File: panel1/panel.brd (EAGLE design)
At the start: 50.1 x 50.4 mm, 31 parts, among them J1 AVR_SPI_PRG_62X3_LOCK, J3 AVR_SPI_PRG_62X3_LOCK

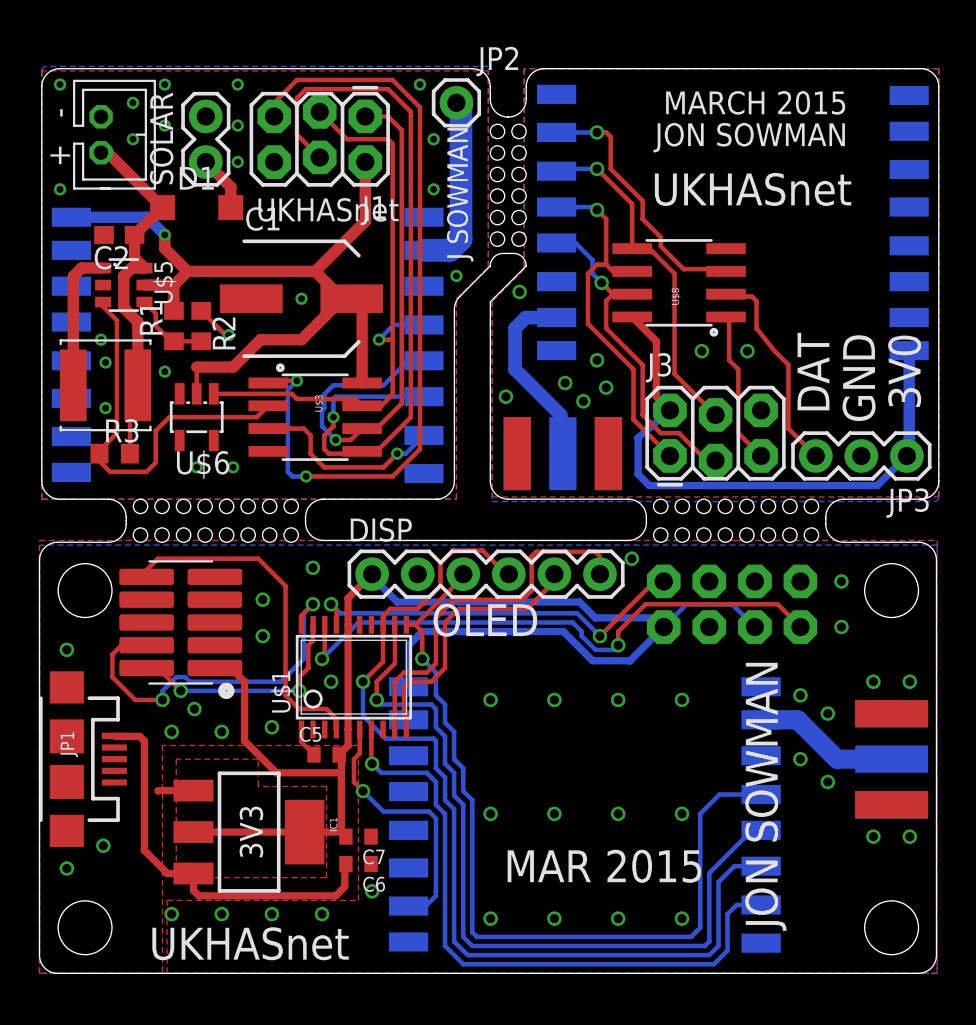
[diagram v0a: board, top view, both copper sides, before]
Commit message: added jumpers because dont trust ebay sellers
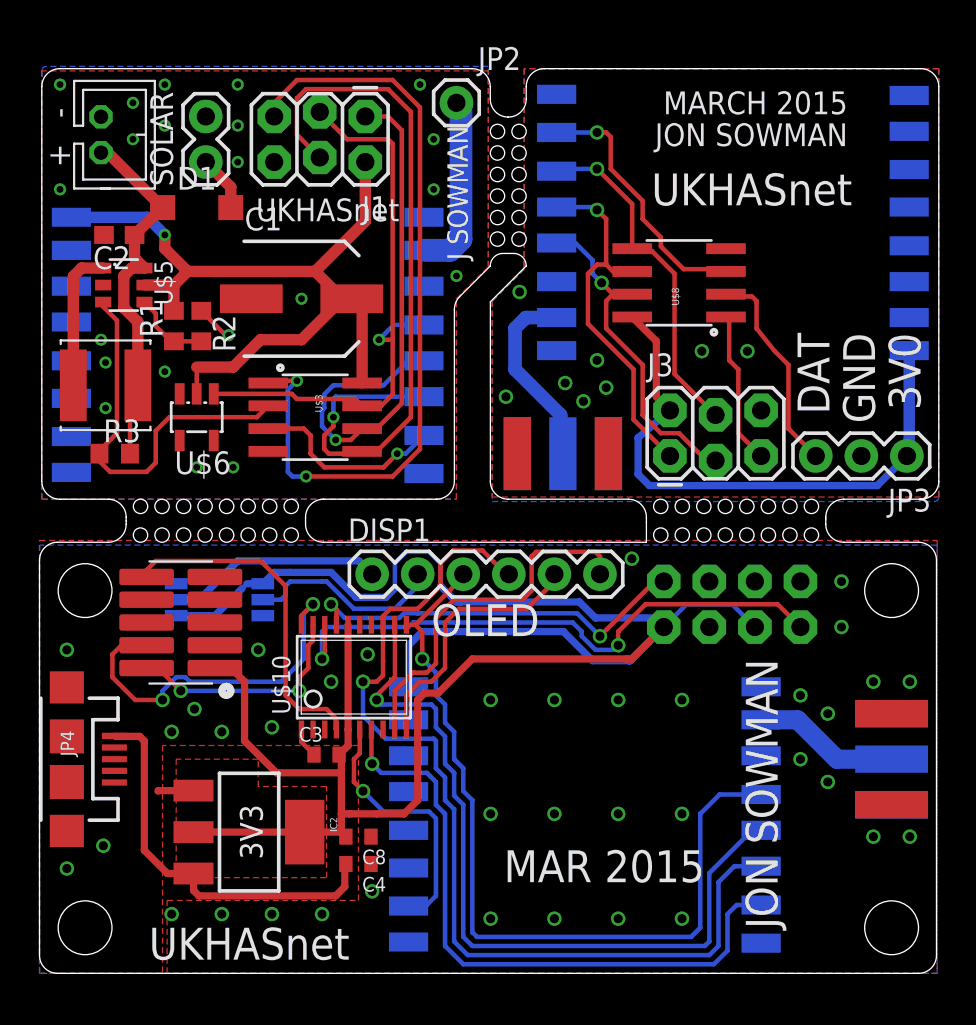
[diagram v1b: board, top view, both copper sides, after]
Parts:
- added SJ1, SJ2: (no value), SparkFun-Retired:SJ_3
- renumbered C5 to C3, C6 to C4, C7 to C8, DISP to DISP1, ESP8266 to ESP1, IC1 to IC2, J$1 to J$3, JP1 to JP4, U$1 to U$10, U$2 to U$11, U$4 to U$12
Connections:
- net DISPLAY_CS renamed DISPLAY_CS1
- net DISPLAY_DC renamed DISPLAY_DC1
- net DISPLAY_RST renamed DISPLAY_RST1
- net MISO renamed MISO3
- net MOSI renamed MOSI3
- net NRST renamed NRST1
- net RFM_CS renamed RFM_CS1
- net SCK renamed SCK2
- net SWCLK renamed SWCLK1
- net SWDAT renamed SWDAT1
- net UART_RX renamed UART_RX1
- net UART_TX renamed UART_TX1
- removed net GND: C3.1, C4.1, C8.1, DISP1.2, ESP1.2, IC2.1, J$3.GND@0, J$3.GND@1, J$3.GND@2, J$3.GND@3, JP4.GND, JP4.MT1, JP4.MT2, U$10.1, U$10.15, U$11.GNDA, U$11.GNDB, U$12.3, U$12.5, U$12.7, U$12.9
- removed net VCC: C3.2, C8.2, DISP1.1, ESP1.3, ESP1.7, IC2.2, IC2.4, U$10.16, U$10.5, U$11.VCC, U$12.1
- new net GND3: C3.1, C4.1, C8.1, ESP1.2, IC2.1, J$3.GND@0, J$3.GND@1, J$3.GND@2, J$3.GND@3, JP4.GND, JP4.MT1, JP4.MT2, SJ1.3, SJ2.3, U$10.1, U$10.15, U$11.GNDA, U$11.GNDB, U$12.3, U$12.5, U$12.7, U$12.9
- new net N$13: DISP1.2, SJ1.2
- new net N$14: DISP1.1, SJ2.2
- new net VCC3: C3.2, C8.2, ESP1.3, ESP1.7, IC2.2, IC2.4, SJ1.1, SJ2.1, U$10.16, U$10.5, U$11.VCC, U$12.1
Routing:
- net VCC3: track 0.00 -> 115.0 mm
- net VCC: track 77.2 -> 0.00 mm
- net N$14: track 0.00 -> 12.1 mm
- net N$13: track 0.00 -> 11.2 mm
- net GND3: track 0.00 -> 3.68 mm, vias 0 -> 38
- net GND: track 3.68 -> 0.00 mm, vias 39 -> 0
- net UART_RX1: track 32.3 -> 33.2 mm
- added copper zone on layer 1, net GND3
- added copper zone on layer 16, net GND3
- added copper zone on layer 1, net VCC3
- removed copper zone on layer 1, net GND
- removed copper zone on layer 16, net GND
- removed copper zone on layer 1, net VCC
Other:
- outline, holes or cut-outs redrawn
- board text added: "P1"
- board text added: "P2"
